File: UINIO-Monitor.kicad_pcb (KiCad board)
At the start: 2 copper layers, 90.8 x 77.9 mm, 57 parts, among them J1 Conn_01x09_Male, J2 Conn_01x09_Male, J3 Conn_01x04_Male, J4 Conn_01x09_Male, P1 LCD_Pad_10Pin, P2 LCD_Pad_12Pin, P3 OLED_Pad_30Pin, P4 LCD_Pad_13Pin, U1 ME6211, U2 ME6211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

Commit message: Prepare UINIO-Monitor version 2.0.0.
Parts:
- added ?: LOGO, LOGO, B.Cu at (116.1, 130.0)
- added ?: LOGO, LOGO, F.Cu at (119.3, 110.3)
- added ?: LOGO, LOGO, F.Cu at (119.1, 130.1)
- added ?: LOGO, LOGO, B.Cu at (116.9, 110.5)
- added FPC5: FPC-SMD_4P-0.5mm, Uinio:FPC-SMD_4P-P0.5, F.Cu at (115.0, 130.1)
- added FPC6: FPC-SMD_10P-0.5mm, Uinio:FPC-SMD_10P-P0.5, F.Cu at (115.0, 110.4)
- added HOLE**: Hole-1mm, Uinio:Hole-1mm, F.Cu at (118.1, 123.4)
- added HOLE**: Hole-1mm, Uinio:Hole-1mm, F.Cu at (188.5, 113.6)
- added HOLE**: Hole-1mm, Uinio:Hole-1mm, F.Cu at (127.1, 73.7)
- added HOLE**: Hole-1mm, Uinio:Hole-1mm, F.Cu at (137.2, 113.6)
- added HOLE**: Hole-1mm, Uinio:Hole-1mm, F.Cu at (127.1, 104.0)
- added J5: Conn_01x04_Male, Connector_PinHeader_2.54mm:PinHeader_1x04_P2.54mm_Vertical, F.Cu at (123.3, 133.9)
- added J6: Conn_01x09_Male, Connector_PinHeader_2.54mm:PinHeader_1x09_P2.54mm_Vertical, F.Cu at (123.3, 120.6)
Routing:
- net Net-(FPC6-Pad2): track 0.00 -> 17.6 mm
- net Net-(FPC6-Pad3): track 0.00 -> 13.8 mm
- net Net-(FPC6-Pad10): track 0.00 -> 13.3 mm
- net Net-(FPC6-Pad4): track 0.00 -> 11.9 mm
- net Net-(FPC6-Pad1): track 0.00 -> 10.9 mm, vias 0 -> 1
- net Net-(FPC6-Pad5): track 0.00 -> 10.1 mm
- net Net-(FPC5-Pad1): track 0.00 -> 8.34 mm
- net Net-(FPC5-Pad4): track 0.00 -> 8.32 mm
- net Net-(FPC6-Pad6): track 0.00 -> 8.18 mm
- net Net-(FPC5-Pad2): track 0.00 -> 7.50 mm
- net Net-(FPC6-Pad8): track 0.00 -> 7.50 mm
- net Net-(FPC5-Pad3): track 0.00 -> 7.47 mm
- net Net-(FPC6-Pad7): track 0.00 -> 7.30 mm
- net GND: track 162.9 -> 168.0 mm, vias 26 -> 30
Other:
- outline, holes or cut-outs redrawn

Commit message: Prepare UINIO-Monitor version 2.0.0.
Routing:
- net GND: vias 30 -> 31

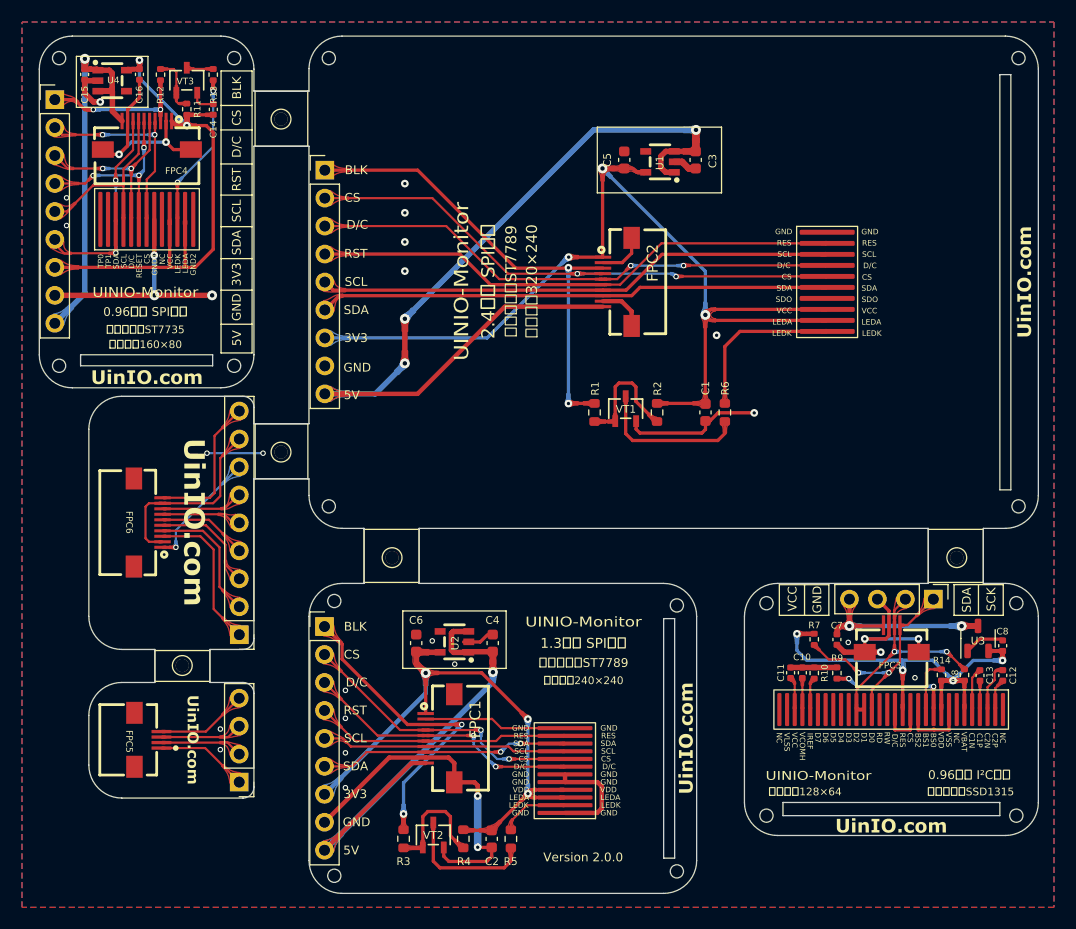
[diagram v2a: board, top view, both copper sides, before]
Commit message: PCB layout update.
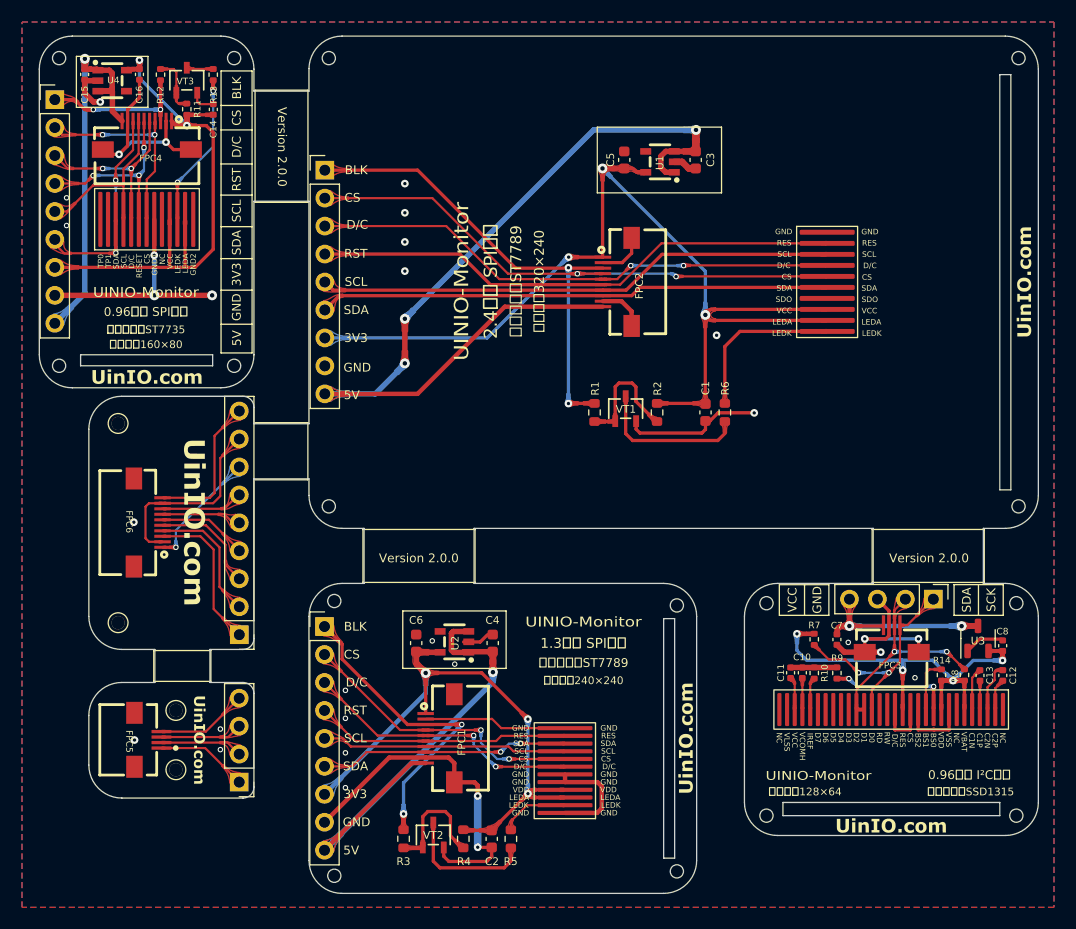
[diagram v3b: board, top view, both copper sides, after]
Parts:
- removed the HOLE** at (118.1, 123.4)
- removed the HOLE** at (188.5, 113.6)
- removed the HOLE** at (127.1, 73.7)
- removed the HOLE** at (137.2, 113.6)
- removed the HOLE** at (127.1, 104.0)
- added HOLE**: Hole-1mm, Uinio:Hole-1mm, F.Cu at (112.3, 119.5)
- added HOLE**: Hole-1mm, Uinio:Hole-1mm, F.Cu at (112.3, 101.4)
- added HOLE**: Hole-1mm, Uinio:Hole-1mm, F.Cu at (117.5, 132.8)
- added HOLE**: Hole-1mm, Uinio:Hole-1mm, F.Cu at (117.5, 127.4)
- moved ? 0.59 mm to (119.7, 130.1)
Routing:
- net GND: track 168.0 -> 162.9 mm
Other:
- outline, holes or cut-outs redrawn

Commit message: Prepare UINIO-Mointor version 2.0.0.
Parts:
- moved ? 0.15 mm to (117.0, 110.5)
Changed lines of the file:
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@@
     (property "Sheetname" "")
     (attr through_hole)
-    (fp_text reference "FPC3" (at -1.190001 2.42) (layer "F.SilkS")
+    (fp_text reference "FPC3" (at -1.210001 1.82) (layer "F.SilkS")
       (effects (font (size 0.6 0.6) (thickness 0.1)) (justify left))
     )
@@
     (pad "13" smd roundrect (at 0.03 4.21 90) (size 5 0.38) (layers "F.Cu" "F.Paste" "F.Mask") (roundrect_rratio 0.25)
       (net 2 "GND") (pinfunction "GND2") (pintype "passive"))
-    (model "${KIPRJMOD}/Libraries/Uinio.3D/xxxxx.step"
-      (offset (xyz -8 2.4 0))
+    (model "${KIPRJMOD}/Libraries/Uinio.3D/0.96Inch-LCD-3D-Model.step"
+      (offset (xyz 2.5 0.1 -2.5))
       (scale (xyz 1 1 1))
-      (rotate (xyz 0 180 -90))
+      (rotate (xyz 0 -180 90))
     )
   )
@@
     (pad "30" smd roundrect (at -0.1 10.01 270) (size 3 0.38) (layers "F.Cu" "F.Paste" "F.Mask") (roundrect_rratio 0.25)
       (net 2 "GND") (pinfunction "NC") (pintype "passive"))
-    (model "${KIPRJMOD}/Libraries/Uinio.3D/0.96Inch-3D-Model.step"
+    (model "${KIPRJMOD}/Libraries/Uinio.3D/0.96Inch-OLED-3D-Model.step"
       (offset (xyz -0.2 0.14 -1.7))
       (scale (xyz 1 1 1))
@@
   )
   (footprint "LOGO" (layer "B.Cu")
-    (at 116.91868 110.45132 90)
+    (at 117.041294 110.545869 90)
     (attr board_only exclude_from_pos_files exclude_from_bom)
     (fp_text reference "" (at 0 0 90) (layer "B.SilkS")
